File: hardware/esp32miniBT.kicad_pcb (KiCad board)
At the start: 2 copper layers, 24.1 x 36.2 mm, 26 parts, among them J1 Conn_02x05_Odd_Even, J4 SolderJumper_2_Open, U1 NCP1117ST33T3G, U2 ESP32-WROOM

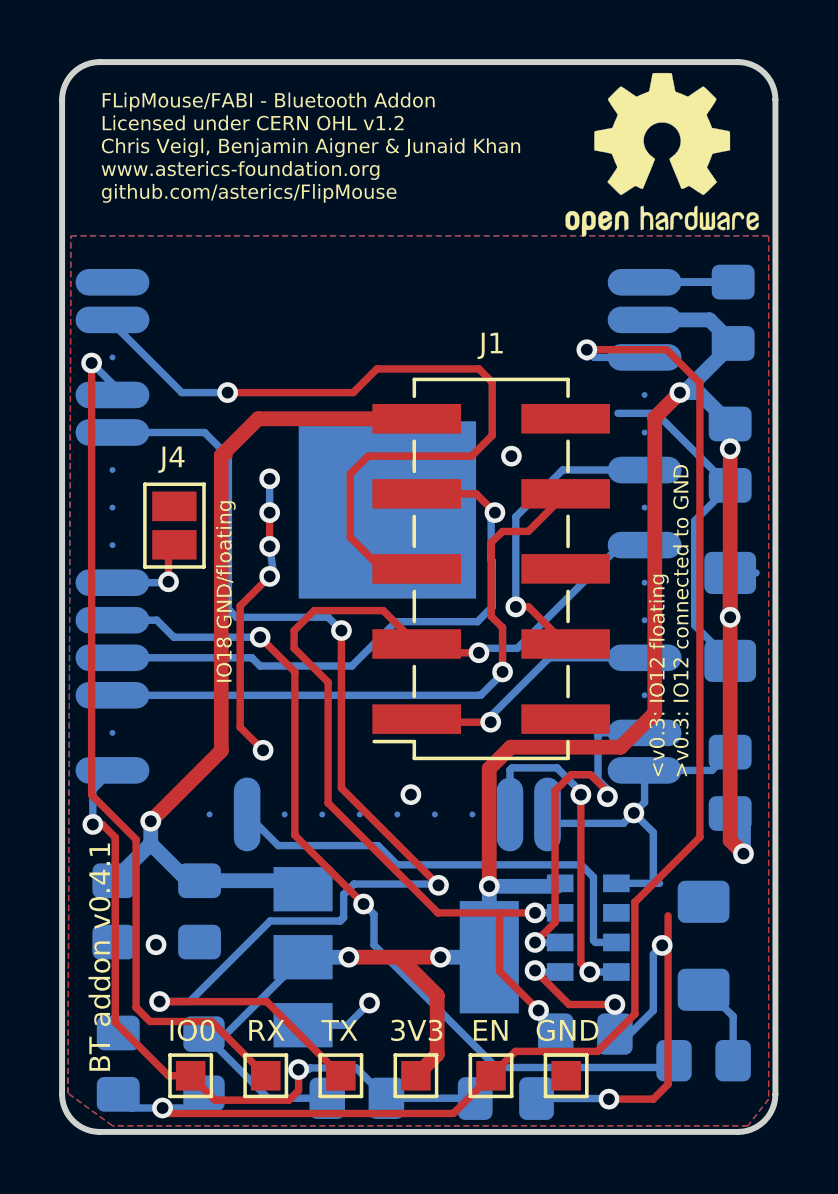
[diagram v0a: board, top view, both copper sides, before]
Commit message: * changed LDO to DCDC (avoiding problems with low USB voltage) * changed IO0 pullup to 10k (avoiding problems with download mode on some ESP32 revisions) * added PDF
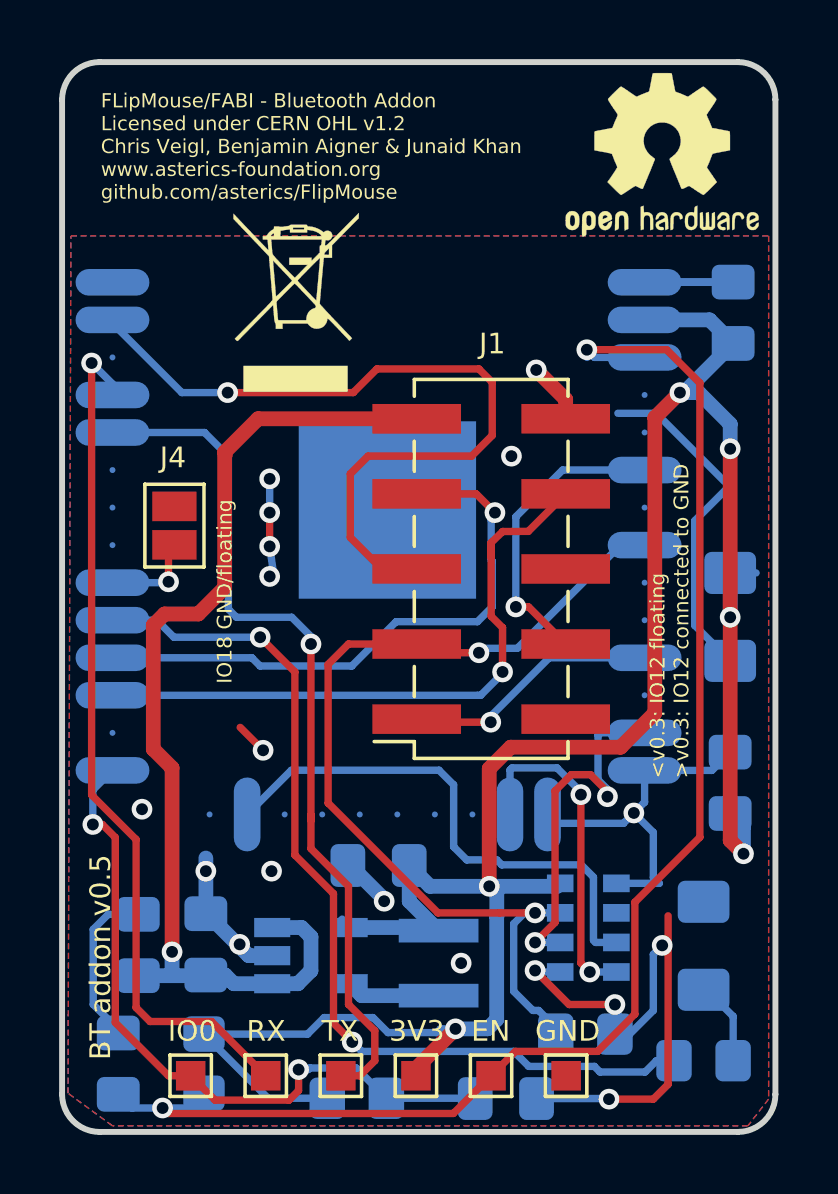
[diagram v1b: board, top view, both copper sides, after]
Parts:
- added L1: 4.7u / TYS30104R7M-10, Inductor_SMD:L_Taiyo-Yuden_MD-3030, B.Cu at (171.2, 92.2)
- added REF**: WEEE-Logo_4.2x6mm_SilkScreen, Symbol:WEEE-Logo_4.2x6mm_SilkScreen, F.Cu at (166.4, 69.8)
- R2: value 100K -> 10k
- U1: value NCP1117ST33T3G -> MCP1603T-330I/OS; footprint Package_TO_SOT_SMD:SOT-223-3_TabPin2 -> Package_TO_SOT_SMD:TSOT-23-5
- moved C3 18.3 mm to (169.2, 88.9), turned to 180 degrees
- moved U1 2.88 mm to (166.9, 91.9)
- moved C4 1.41 mm to (161.0, 91.6), turned to 90 degrees
- moved C5 1.14 mm to (163.3, 91.6), turned to 90 degrees
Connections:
- J1 pad 2: Net-(J1-Pad2) -> (no net)
- J1 pad 6: Net-(J1-Pad6) -> (no net)
- U1 pad 1: GND -> VCC
- U1 pad 2: +3V3 -> GND
- U2 pad 10: IO25 -> (no net)
- U2 pad 12: IO27 -> (no net)
- U2 pad 17: Net-(U2-Pad17) -> (no net)
- U2 pad 18: Net-(U2-Pad18) -> (no net)
- U2 pad 19: Net-(U2-Pad19) -> (no net)
- U2 pad 20: Net-(U2-Pad20) -> (no net)
- U2 pad 21: Net-(U2-Pad21) -> (no net)
- U2 pad 22: Net-(U2-Pad22) -> (no net)
- U2 pad 24: IO2 -> (no net)
- U2 pad 26: IO4 -> (no net)
- U2 pad 31: IO19 -> (no net)
- U2 pad 32: Net-(U2-Pad32) -> (no net)
- U2 pad 33: IO21 -> (no net)
- U2 pad 36: IO22 -> (no net)
- U2 pad 4: SVP -> (no net)
- U2 pad 5: SVN -> (no net)
- U2 pad 7: IO35 -> (no net)
- U2 pad 9: IO33 -> (no net)
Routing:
- net TXDtoRXD0: track 42.3 -> 29.8 mm, vias 3 -> 1
- net +3V3: track 74.7 -> 82.7 mm, vias 7 -> 6
- net VCC: track 29.2 -> 35.6 mm
- net GND: track 65.8 -> 72.2 mm, vias 14 -> 18
- net Net-(L1-Pad1): track 0.00 -> 3.18 mm
- net IO32: track 35.0 -> 32.2 mm, vias 3 -> 2
- net IO5: track 31.8 -> 34.6 mm
- net IO15: track 15.5 -> 18.0 mm
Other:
- board text added: "BT addon v0.5"
- board text removed: "BT addon v0.4.1"
